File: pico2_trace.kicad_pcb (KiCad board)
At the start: 2 copper layers, 92 x 64 mm, 56 parts, among them J10 SWD, J1B BREAKOUT, J2B BREAKOUT, J3 MIPI-20, J5 USB-A HOST, J6 CORTEX-10, J7 JST-SH-3 DEBUG_PROBE, J8 USB-MICROB PWR, J9 USB-MICROB DEV, SW1 RESET

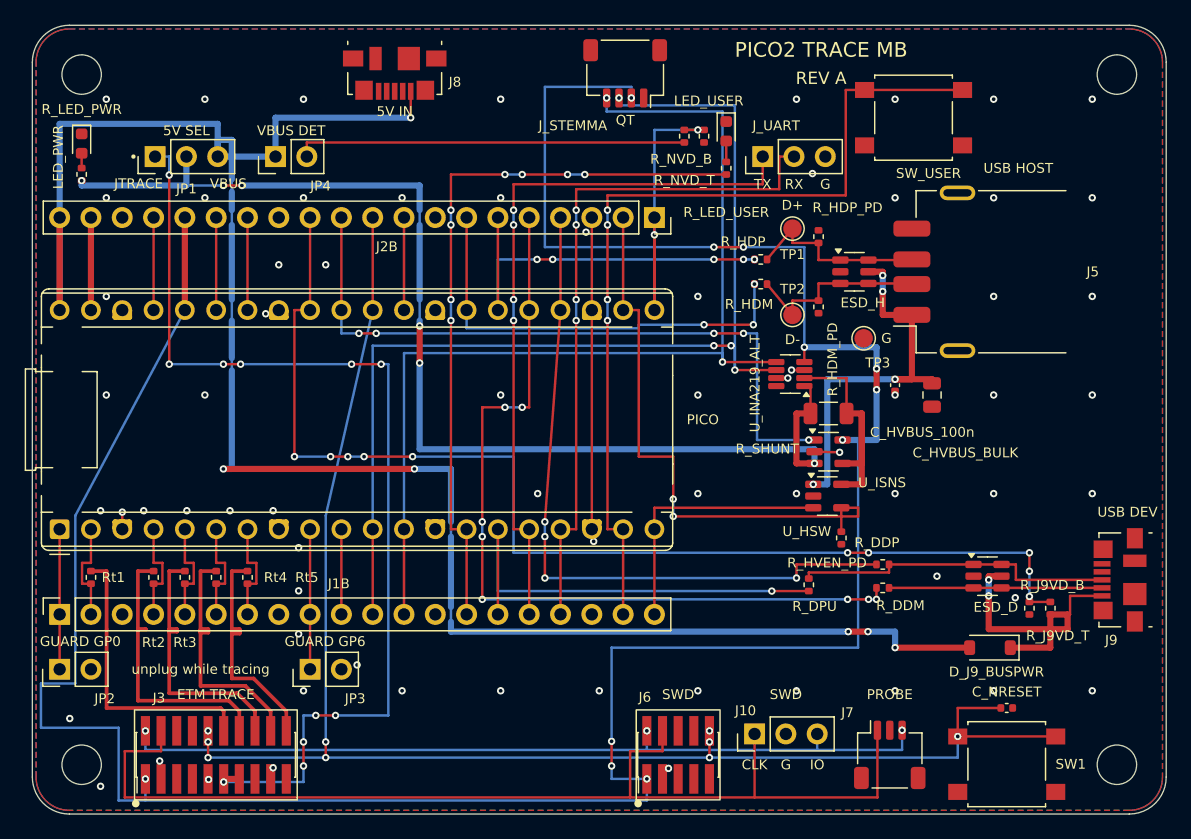
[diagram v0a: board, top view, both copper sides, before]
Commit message: pcb: fix diode direction, ground J5 shell, add VSYS feed + decoupling, widen V5_JTRACE
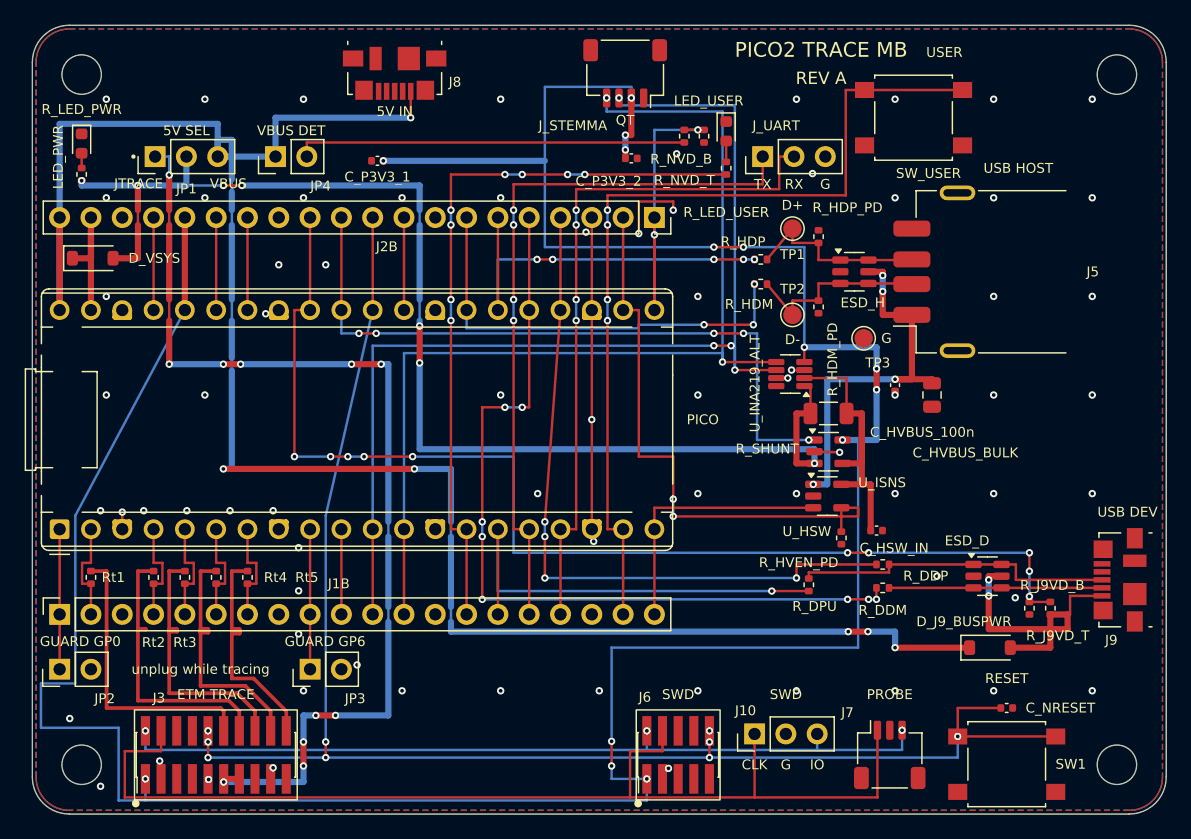
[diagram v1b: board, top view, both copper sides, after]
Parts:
- added C_HSW_IN: 100n/16V, C_0402_1005Metric, F.Cu at (68.5, 41.0)
- added C_P3V3_1: 100n/16V, C_0402_1005Metric, F.Cu at (28.0, 11.0)
- added C_P3V3_2: 100n/16V, C_0402_1005Metric, F.Cu at (48.6, 10.8)
- added D_VSYS: B5819W, D_SOD-123, F.Cu at (4.90, 18.9)
- turned D_J9_BUSPWR to 0 degrees
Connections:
- D_J9_BUSPWR pad 1: J9_VBUS -> VBUS_NET
- D_J9_BUSPWR pad 2: VBUS_NET -> J9_VBUS
- J5 pad 5: (no net) -> GND
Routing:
- net P3V3: track 224.0 -> 242.5 mm, vias 11 -> 14
- net VBUS_SEL: track 94.1 -> 102.0 mm, vias 6 -> 7
- net GND: track 30.8 -> 36.9 mm, vias 69 -> 73
- net VSYS: track 7.51 -> 12.3 mm
- net HOST_5V_IN: track 20.6 -> 25.0 mm
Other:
- board text added: "RESET"
- board text added: "USER"

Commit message: pcb: J8 micro-B -> USB Type-C power input (C165948) + CC pull-downs
- usb_c_pwr footprint: local renumbered copy of the stock HRO
  TYPE-C-31-M-12 land (1=VBUS A4/B9, 2=CC1, 3=CC2, 4=GND, 5=NC data/SBU,
  6=shield, 7=VBUS A9/B4 second column, board-NC: the NPTH peg blocks
  every legal escape; the plug parallels all four VBUS beams)
- R_CC1/R_CC2 5.1k Rd (C25905) west of the connector; CC stubs run
  north out of the pad row and west under the body (crossing-free lane
  pair y=5.25/5.7, DRC-derived)
- VBUS_NET approach corridor moved y=7.5 -> 5.0 (old lane is under the
  new pad row); pour stitch via (22.0,6.0) -> (23.6,6.9)
- board regenerated from scratch (pipeline first proven byte-equivalent
  vs the frozen 6d67559 board); gates: DRC 0 unconnected + 2 known silk
  warnings, ERC warnings-only, netlists match, pour union-find = 1
  component, checks 7/7
- BOM/BOM_jlc/CPL_jlc/DESIGN/ORDERING updated; new fab zip
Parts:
- added R_CC1: 5.1k, R_0402_1005Metric, F.Cu at (21.3, 6.90)
- added R_CC2: 5.1k, R_0402_1005Metric, F.Cu at (22.6, 6.90)
- J8: value USB-MICROB PWR -> USB-C PWR; footprint USB_Micro-B_Molex_47346-0001 -> USB_C_PWR_HRO_TYPE-C-31-M-12
- moved J8 0.25 mm to (29.4, 4.15)
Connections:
- J8 pad 2: (no net) -> J8_CC1
- J8 pad 3: (no net) -> J8_CC2
- J8 pad 4: (no net) -> GND
- J8 pad 5: GND -> (no net)
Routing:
- net J8_CC1: track 0.00 -> 13.4 mm
- net J8_CC2: track 0.00 -> 8.23 mm
- net VBUS_NET: track 164.0 -> 168.6 mm

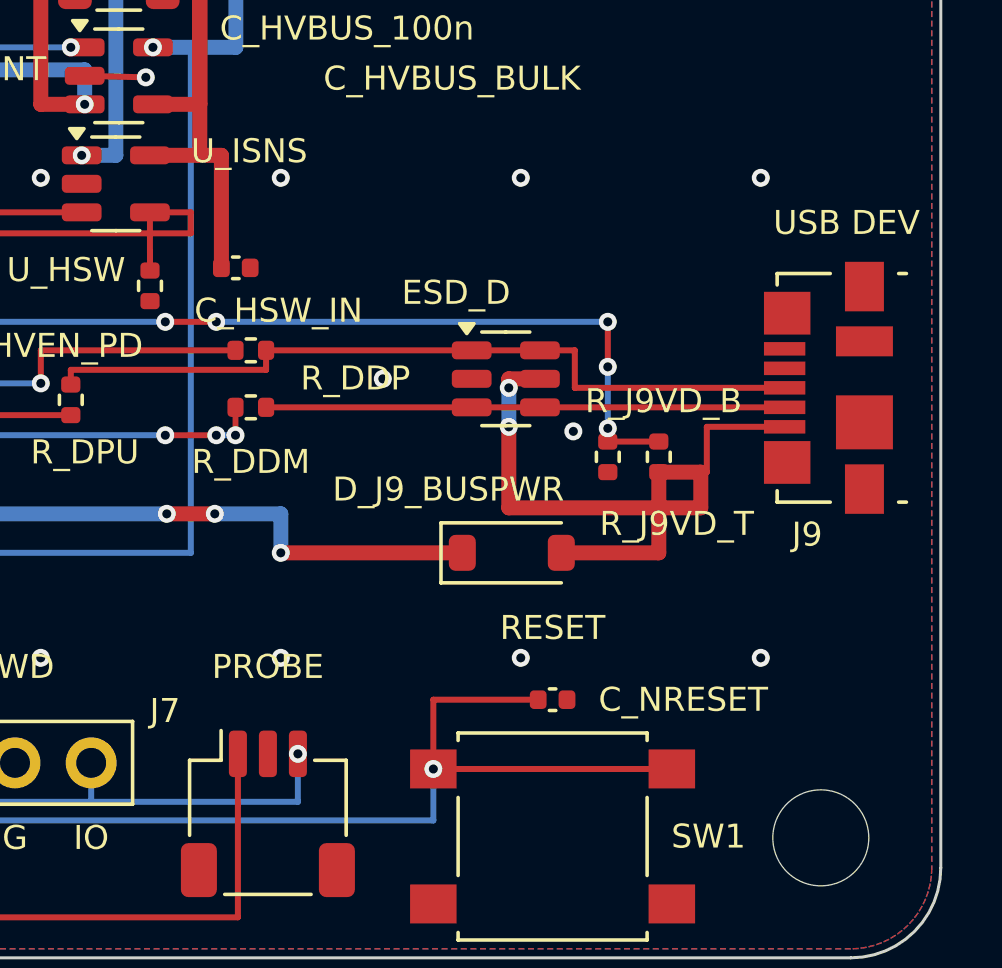
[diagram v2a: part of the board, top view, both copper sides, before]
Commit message: pcb: J9 micro-B -> USB Type-C device port (C165948) + CC pull-downs
- usb_c_dev footprint: renumbered HRO land for a USB2 device (1=VBUS,
  2/3=CC, 4=GND, 5=D+ A6/B6, 6=D- A7/B7, 7=SBU nc, 8=second VBUS column
  board-NC, 9=shield)
- interleaved D+/D- pairs bridged with a two-layer weave (D- rail on F,
  D+ through B via pair threading the NPTH peg gap)
- R_CC3/R_CC4 Rd + the VBUS-detect divider relocated to the south band;
  DEV_VBUS_DET tail re-derived (east B_Cu descent at x=86.2); J9_VBUS
  web rebuilt (spine y=54.4, ESD_D.5 tap around the DM wall on B_Cu)
- pour: 1 stale fragment via moved, 2 new stitch vias for the boxed-in
  R_CC4.2/R_J9VD_B.2 ground pockets
- gates: DRC 0 unconnected + 2 baseline silk warnings, checks 7/7, ERC
  warnings-only, netlists match, pour union-find 1 component (39 islands,
  75 vias)
- last micro-B eliminated: C132560 drops from the BOM entirely
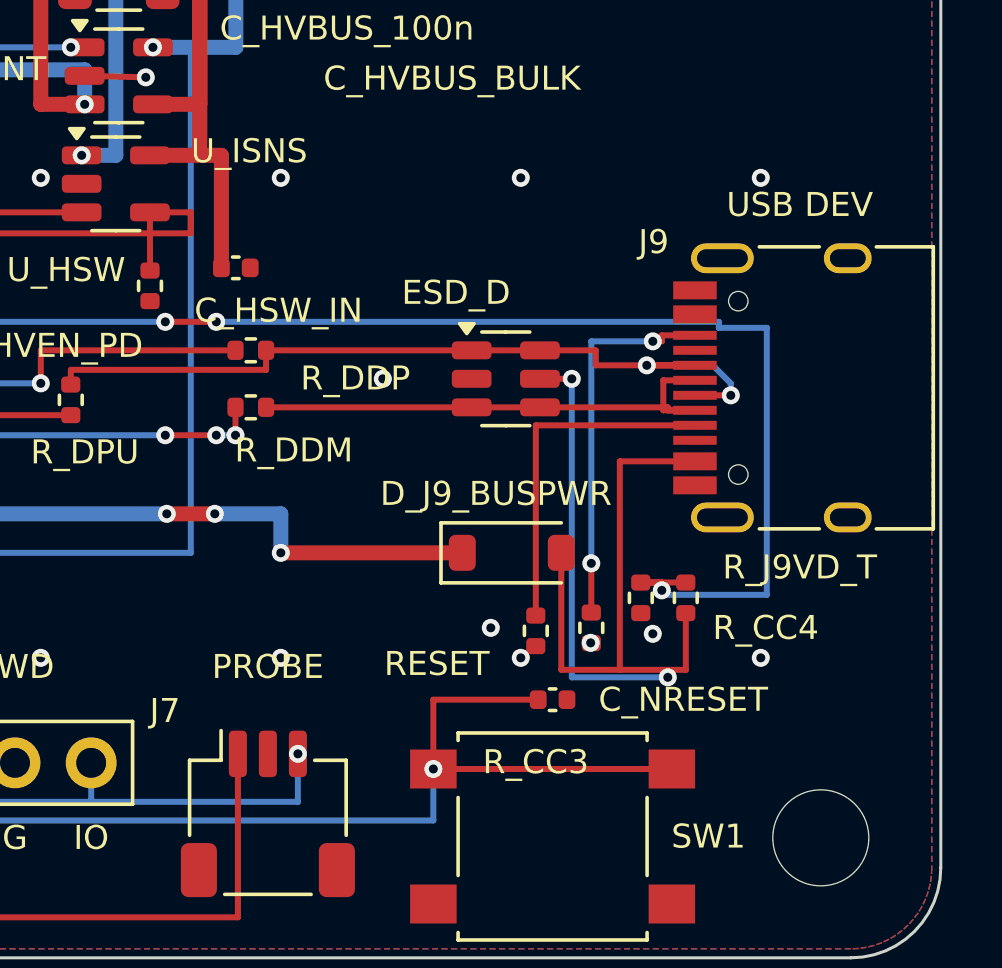
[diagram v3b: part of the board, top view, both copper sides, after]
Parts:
- added R_CC3: 5.1k, R_0402_1005Metric, F.Cu at (78.5, 53.1)
- added R_CC4: 5.1k, R_0402_1005Metric, F.Cu at (80.3, 53.0)
- J9: value USB-MICROB DEV -> USB-C DEV; footprint USB_Micro-B_Molex_47346-0001 -> USB_C_DEV_HRO_TYPE-C-31-M-12
- moved R_J9VD_B 4.83 mm to (82.0, 52.0)
- moved R_J9VD_T 4.79 mm to (83.5, 52.0)
- moved J9 0.41 mm to (87.8, 45.0)
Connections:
- J9 pad 2: DEV_DM -> J9_CC1
- J9 pad 3: DEV_DP -> J9_CC2
- J9 pad 4: (no net) -> GND
- J9 pad 5: GND -> DEV_DP
- J9 pad 6: GND -> DEV_DM
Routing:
- net DEV_VBUS_DET: track 93.8 -> 108.6 mm, vias 10 -> 8
- net J9_CC2: track 0.00 -> 12.7 mm, vias 0 -> 2
- net J9_CC1: track 0.00 -> 11.6 mm
- net J9_VBUS: track 26.0 -> 33.8 mm
- net DEV_DP: track 26.2 -> 28.7 mm, vias 0 -> 2
- net GND: vias 73 -> 75
